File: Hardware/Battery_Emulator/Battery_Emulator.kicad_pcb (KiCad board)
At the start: 2 copper layers, 48 parts, among them J1 Vin, J2 USB4105-GF-A-060, Q1 IRFB7545PBF, SW1 Jumper, SW2 Jumper, U1 MCP4651T-103E_ST, U10 ATmega328PB-A, U2 ISO1640BDR, U3 74AHC2G125DP,125, U4 FT230XS-R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

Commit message: Update PCB
Made PCB in Kicad
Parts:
- added C22: 100n, Capacitor_SMD:C_0805_2012Metric, F.Cu at (53.3, 59.1)
- added J3: Cell1_Vout, TerminalBlock_Phoenix:TerminalBlock_Phoenix_MKDS-1,5-2-5.08_1x02_P5.08mm_Horizontal, F.Cu at (58.1, 132.7)
- J1: footprint Connector_PinSocket_2.00mm:PinSocket_1x02_P2.00mm_Vertical -> TerminalBlock_Phoenix:TerminalBlock_Phoenix_MKDS-1,5-2-5.08_1x02_P5.08mm_Horizontal
- Q1, U7: moved to B.Cu
- RV3, RV4: footprint Potentiometer_THT:Potentiometer_Bourns_PTA3043_Single_Slide -> Connector_PinHeader_2.54mm:PinHeader_1x03_P2.54mm_Vertical
- moved J2 102.7 mm to (48.5, 51.8), turned to 180 degrees
- moved R6 97.3 mm to (43.8, 58.5)
- moved C14 94.8 mm to (43.7, 60.5)
- moved RV3 91.1 mm to (69.4, 110.8)
- moved U4 89.8 mm to (48.9, 60.5), turned to 180 degrees
- moved Q1 80.1 mm to (62.3, 124.1), turned to 90 degrees
- moved C11 79.4 mm to (53.4, 62.6)
- moved C12 75.0 mm to (54.5, 70.3), turned to 0 degrees
- moved C9 74.5 mm to (51.0, 70.3), turned to 180 degrees
- moved U5 73.4 mm to (46.5, 67.8), turned to 0 degrees
- moved RV4 66.7 mm to (70.2, 94.1)
- moved C10 66.2 mm to (47.6, 70.3), turned to 0 degrees
- moved U7 66.1 mm to (62.3, 113.4), turned to 90 degrees
- moved C13 66.1 mm to (44.2, 70.3), turned to 180 degrees
- moved C21 64.8 mm to (66.8, 64.3), turned to 180 degrees
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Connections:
- J2 pad VBUS: +5V -> unconnected-(J2-PadVBUS)
- U1 pad 2: /SCL -> /Cell_1/SCL_ISO
- U1 pad 3: /SDA_cell_1-7 -> /Cell_1/SDA_ISO
- U2 pad 6: /SCL -> /Cell_1/SCL_ISO
- U2 pad 7: /SDA_cell_1-7 -> /Cell_1/SDA_ISO
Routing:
- net +5V: track 0.00 -> 84.9 mm, vias 0 -> 5
- net /Cell_1/COUT+: track 0.00 -> 55.5 mm, vias 0 -> 1
- net /Cell_1/+5V_ISO: track 0.00 -> 51.9 mm
- net /Cell_1/+9V_ISO: track 0.00 -> 38.2 mm
- net Net-(SW2-A): track 0.00 -> 32.8 mm, vias 0 -> 1
- net +12V: track 0.00 -> 27.7 mm
- net Net-(Q1-Pad1): track 0.00 -> 26.8 mm
- net /SCL: track 0.00 -> 25.3 mm, vias 0 -> 2
- net /SDA_cell_1-7: track 0.00 -> 24.9 mm
- net Net-(U8A--): track 0.00 -> 24.3 mm, vias 0 -> 1
- net Net-(SW2-C): track 0.00 -> 17.2 mm, vias 0 -> 2
- net /Cell_1/GND_ISO: track 0.00 -> 17.1 mm, vias 0 -> 7
- net /SDA: track 0.00 -> 15.9 mm, vias 0 -> 2
- net /TX: track 0.00 -> 15.2 mm, vias 0 -> 2
- net /RX: track 0.00 -> 14.1 mm, vias 0 -> 2
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- added copper zone on B.Cu, net /Cell_1/GND_ISO
- added copper zone on F.Cu, net /Cell_1/GND_ISO
- added copper zone on B.Cu, net GND
- added copper zone on F.Cu, net GND
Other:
- board outline added: 33 x 89.1 mm

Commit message: Update PCB design
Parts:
- removed U6: LM7805_TO220, Package_TO_SOT_THT:TO-220-3_Vertical
- added U9: KA78M05_TO252, Package_TO_SOT_SMD:TO-252-2, F.Cu at (59.8, 76.8)
- U5: value LM7805_TO220 -> KA78M05_TO252; footprint Package_TO_SOT_THT:TO-220-3_Vertical -> Package_TO_SOT_SMD:TO-252-2
- moved U5 38.0 mm to (57.1, 104.3), turned to 180 degrees
- moved C12 13.0 mm to (55.8, 83.3)
- moved C9 12.0 mm to (55.8, 81.3), turned to 0 degrees
- moved C1 11.3 mm to (64.6, 106.1)
- moved C10 7.80 mm to (55.1, 72.3)
- moved C13 7.52 mm to (51.7, 70.8)
- moved C21 3.85 mm to (67.2, 68.2)
- moved C22 3.85 mm to (53.8, 63.0)
- moved C4 3.85 mm to (67.3, 56.8)
- moved C5 3.85 mm to (70.0, 60.2)
- moved C8 3.85 mm to (66.5, 65.2)
- moved R3 3.85 mm to (62.1, 70.8)
- moved R4 3.85 mm to (58.2, 71.2)
- moved R5 3.85 mm to (60.2, 71.2)
- moved R6 3.85 mm to (44.2, 62.4)
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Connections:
- U5 pad 1: +12V -> /Cell_1/+9V_ISO
- U5 pad 2: GND -> /Cell_1/GND_ISO
- U5 pad 3: +5V -> /Cell_1/+5V_ISO
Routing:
- net /Cell_1/+5V_ISO: track 51.9 -> 41.8 mm, vias 0 -> 2
- net Net-(Q1-Pad1): track 26.8 -> 31.5 mm
- net GND: track 13.2 -> 17.7 mm
- net +5V: track 84.9 -> 89.0 mm, vias 5 -> 6
- net /Cell_1/+9V_ISO: track 38.2 -> 42.0 mm
- net +12V: track 27.7 -> 30.2 mm
- net /Cell_1/COUT+: track 55.5 -> 57.8 mm
- net Net-(SW2-C): track 17.2 -> 19.6 mm
- net Net-(U8A--): track 24.3 -> 26.6 mm
- net Net-(U1-P0B): track 14.1 -> 12.3 mm
- net /Cell_1/GND_ISO: track 17.1 -> 18.8 mm, vias 7 -> 9
- net /SDA_cell_1-7: track 24.9 -> 23.6 mm
- net Net-(SW1-B): track 7.61 -> 6.42 mm
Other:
- board size 33 x 89.1 mm -> 33 x 87.2 mm

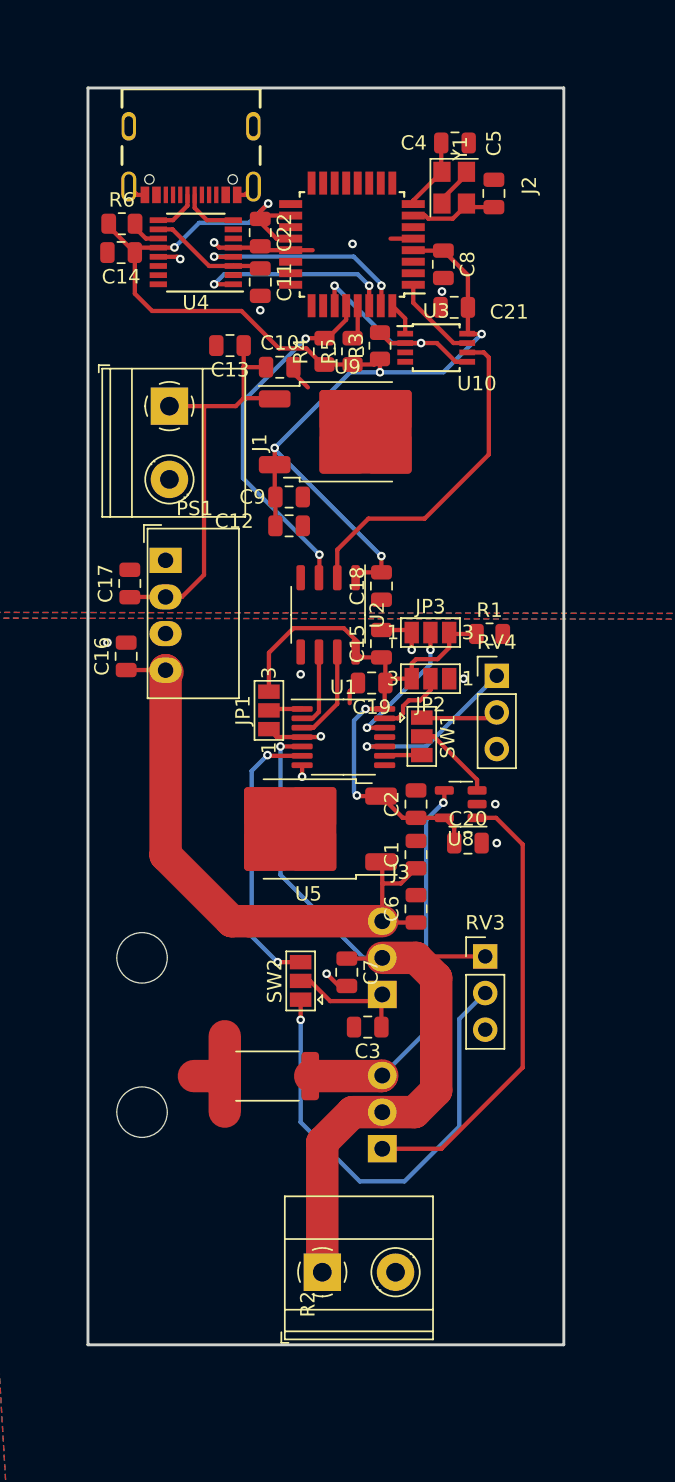
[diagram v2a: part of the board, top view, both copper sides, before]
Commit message: Update PCB
Made traces a lot larger to pass more current.
Added resistor to gate of current sink MOSFET.
Made the gerber files and ordered it at SMD lab.
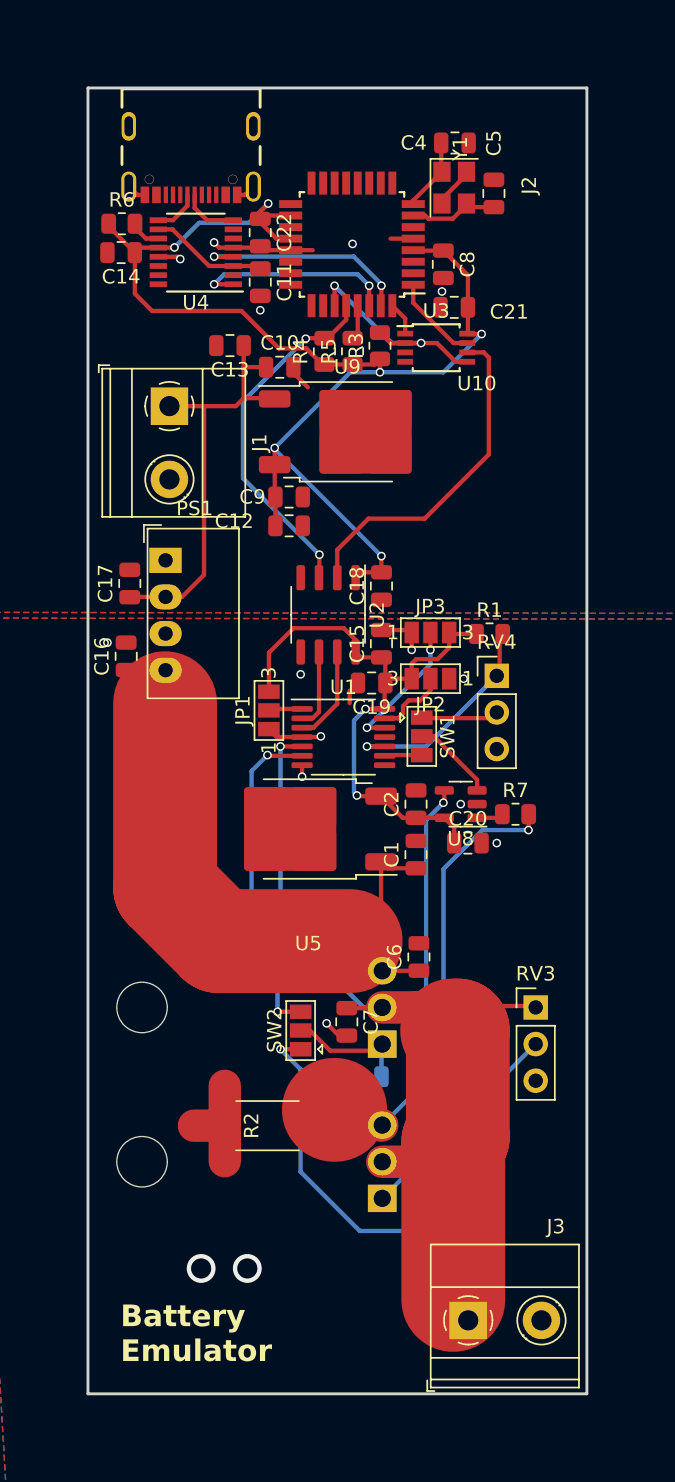
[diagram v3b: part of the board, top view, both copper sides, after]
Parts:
- added R7: 47, Resistor_SMD:R_0805_2012Metric, F.Cu at (71.5, 103.3)
- C3: moved to B.Cu
- moved J3 10.7 mm to (68.2, 138.4)
- moved RV3 4.98 mm to (72.9, 116.7)
- moved R2 3.44 mm to (54.3, 124.9)
- moved C3 3.44 mm to (61.2, 121.5)
- moved C7 3.44 mm to (59.8, 117.7)
- moved Q1 3.44 mm to (62.3, 129.9)
- moved SW2 3.44 mm to (56.6, 118.3)
- moved U7 3.44 mm to (62.3, 119.2)
- moved C6 3.35 mm to (64.8, 113.2)
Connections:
- U8 pad 1: Net-(Q1-Pad1) -> Net-(R7-Pad1)
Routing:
- net /Cell_1/COUT+: track 57.8 -> 76.5 mm
- net Net-(SW2-C): track 19.6 -> 23.0 mm
- net Net-(SW2-A): track 32.8 -> 36.1 mm
- net Net-(U1-P0B): track 12.3 -> 15.3 mm
- net /Cell_1/+9V_ISO: track 42.0 -> 44.7 mm
- net Net-(R7-Pad1): track 0.00 -> 1.85 mm
- net Net-(U8A--): track 26.6 -> 25.1 mm
- net Net-(Q1-Pad1): track 31.5 -> 32.7 mm, vias 0 -> 1
- net /Cell_1/GND_ISO: vias 9 -> 11
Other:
- board size 33 x 87.2 mm -> 34.6 x 90.6 mm
- board text added: "Battery Emulator"

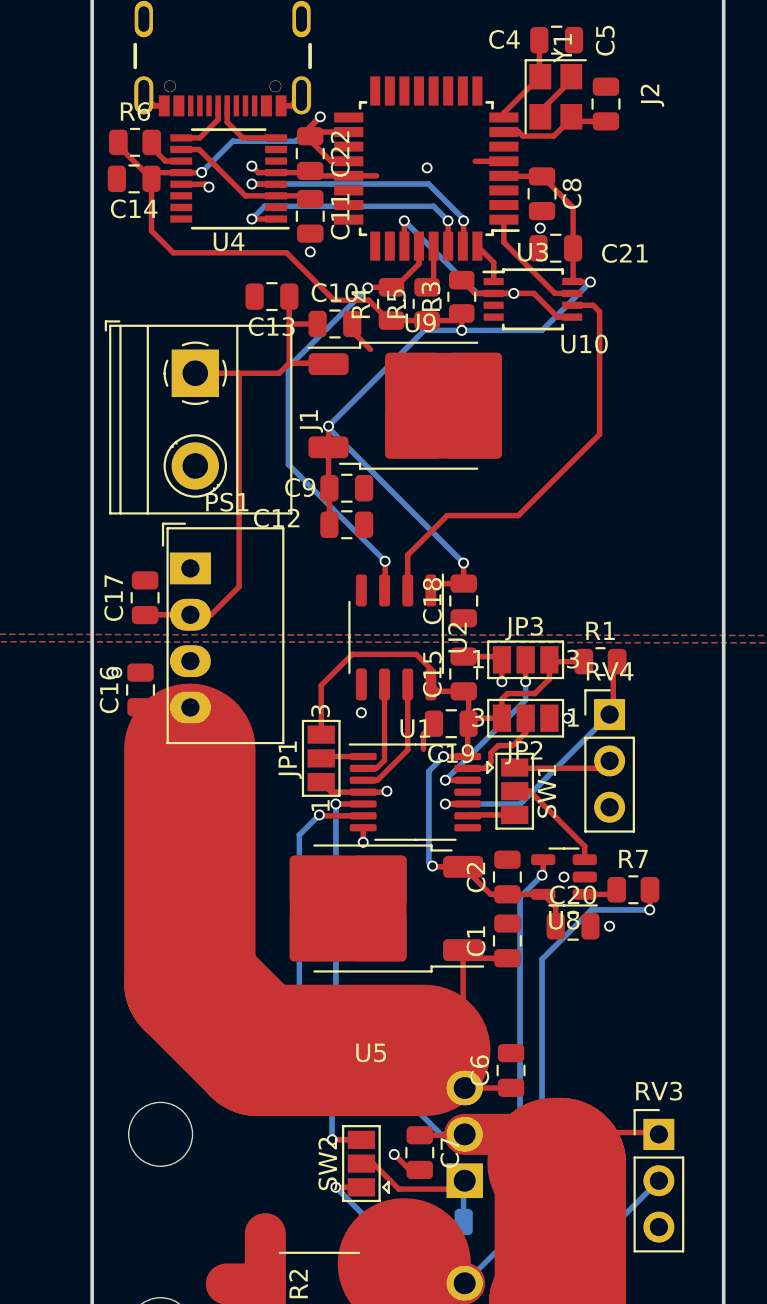
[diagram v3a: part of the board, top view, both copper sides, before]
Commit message: Update PCB
Changed via hole sizes to 0.6mm so it can be made in SMD lab
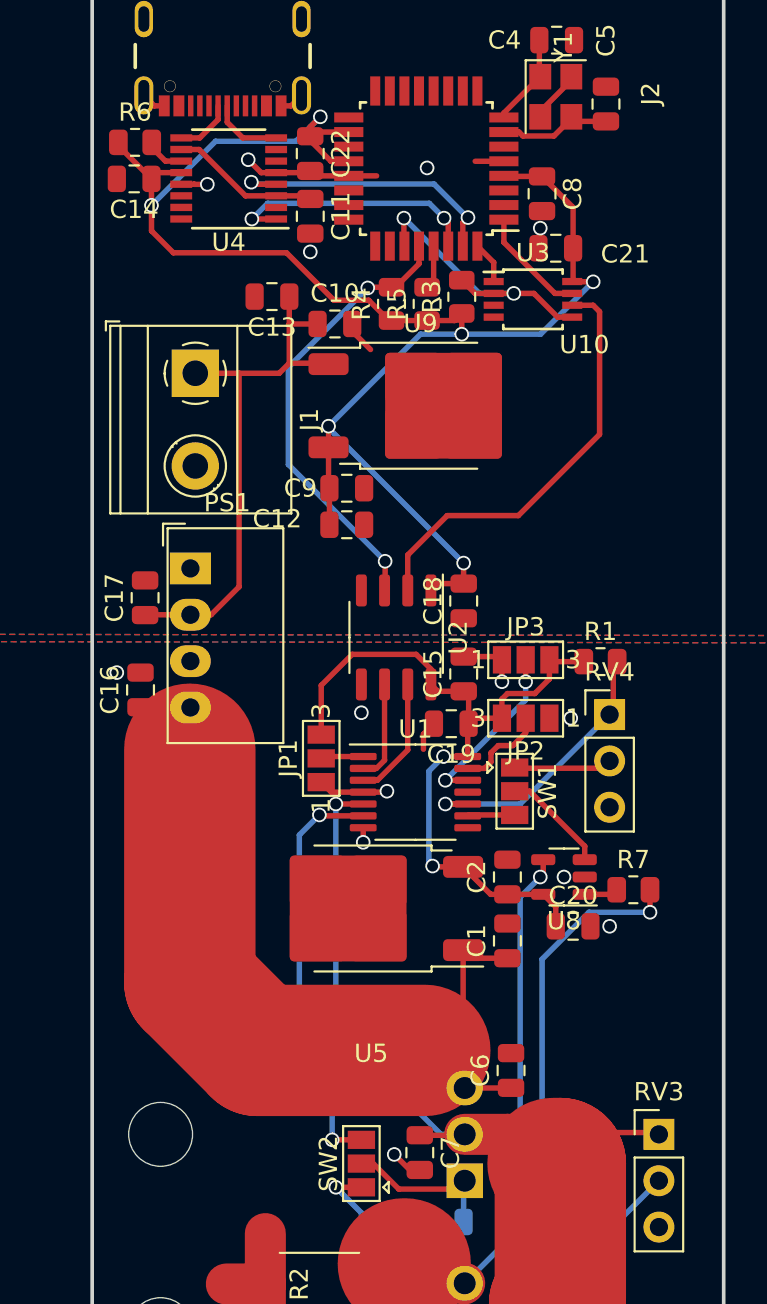
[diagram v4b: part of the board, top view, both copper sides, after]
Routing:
- net +5V: track 89.0 -> 91.9 mm
- net /TX: track 15.2 -> 15.8 mm

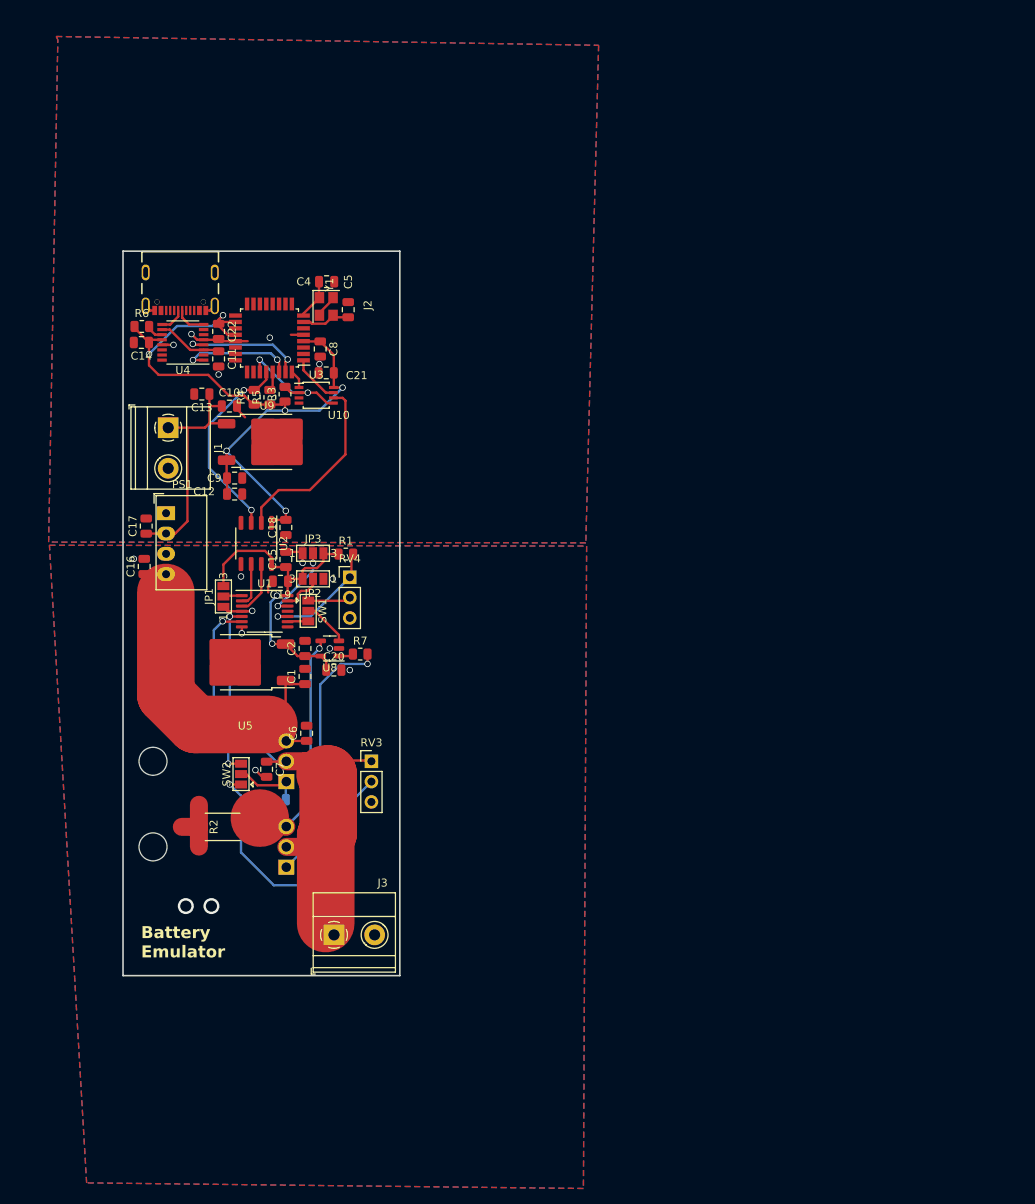
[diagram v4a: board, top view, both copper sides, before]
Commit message: Update PCB
Updated the via sizes to 0.8mm in v1
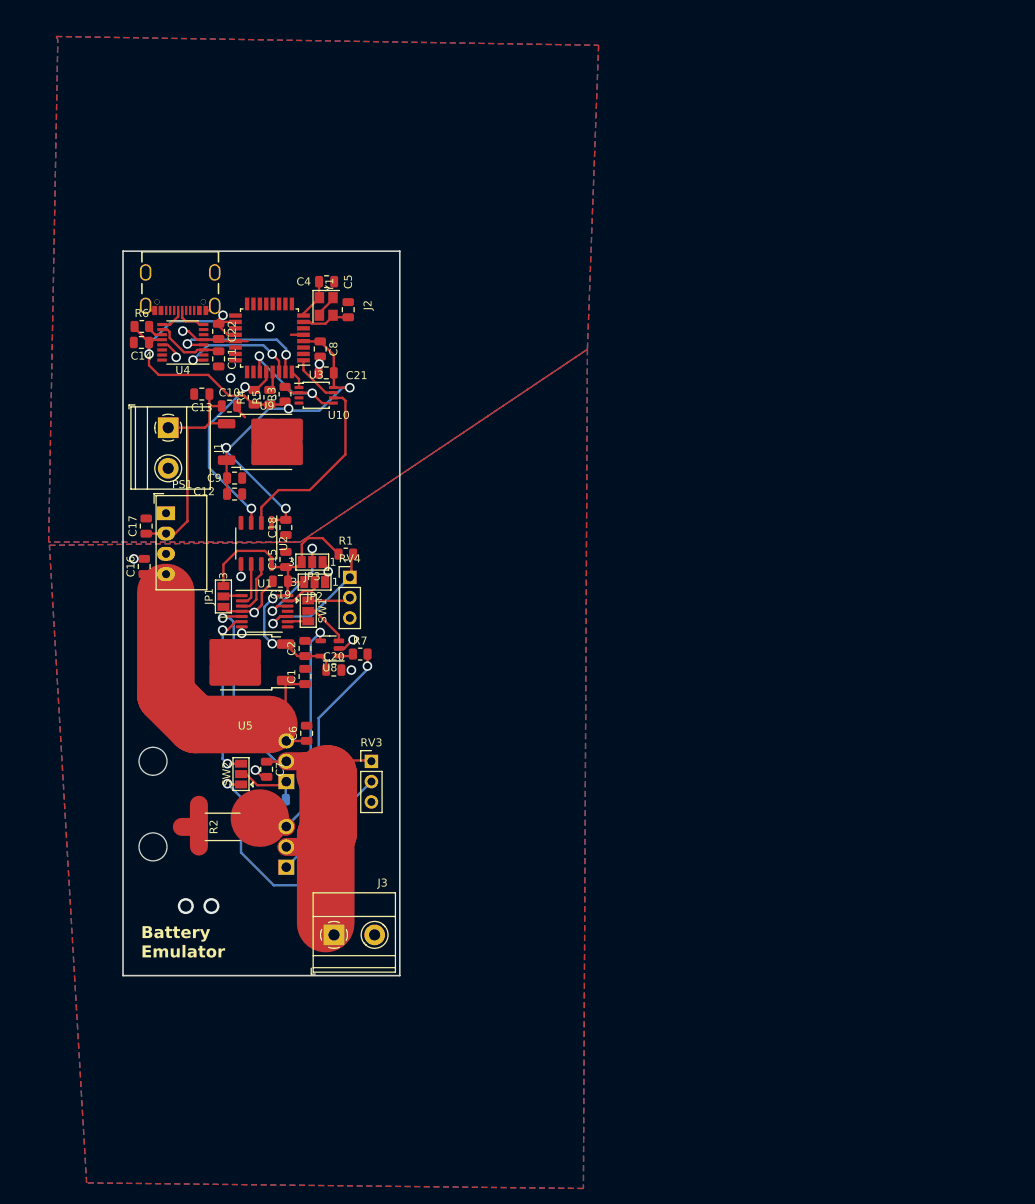
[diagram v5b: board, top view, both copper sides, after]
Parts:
- moved JP3 1.10 mm to (65.5, 91.8), turned to 180 degrees
- moved JP2 0.45 mm to (65.8, 94.3)
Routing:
- net /Cell_1/GND_ISO: track 18.8 -> 24.5 mm, vias 11 -> 10
- net /Cell_1/A2: track 9.65 -> 13.8 mm
- net /Cell_1/+5V_ISO: track 41.8 -> 45.8 mm
- net +5V: track 91.9 -> 95.4 mm
- net GND: track 17.9 -> 20.4 mm
- net /TX: track 15.8 -> 18.0 mm
- net Net-(U8A--): track 25.1 -> 27.2 mm
- net Net-(Q1-Pad1): track 32.8 -> 30.8 mm
- net Net-(U1-P0B): track 15.3 -> 17.3 mm
- net /Cell_1/COUT+: track 76.5 -> 78.1 mm
- net Net-(SW2-C): track 23.0 -> 21.5 mm
- net /SDA: track 16.2 -> 17.7 mm
- net /RX: track 14.2 -> 15.0 mm
- net Net-(U4-3V3OUT): track 8.21 -> 8.89 mm
- net /SCL: track 24.9 -> 25.5 mm
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
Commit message: PCB-update for production
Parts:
- C7: moved to B.Cu
- moved C7 5.59 mm to (65.3, 116.7), turned to 0 degrees
- moved C3 4.63 mm to (65.3, 119.2), turned to 0 degrees
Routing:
- net /Cell_1/GND_ISO: track 24.5 -> 30.5 mm, vias 10 -> 9
- net +5V: track 95.4 -> 100.6 mm
- net /Cell_1/+5V_ISO: track 45.8 -> 48.7 mm
- net /Cell_1/COUT+: track 78.1 -> 80.7 mm, vias 1 -> 2
- net Net-(U8A--): track 27.2 -> 28.9 mm
- net /RX: track 15.0 -> 16.3 mm
- net Net-(U1-P0B): track 17.3 -> 18.4 mm
- net GND: track 20.4 -> 21.4 mm, vias 5 -> 6
- net /TX: track 18.0 -> 18.9 mm
- net Net-(SW2-A): track 36.7 -> 37.5 mm
- net Net-(SW2-B): track 8.80 -> 8.23 mm
- net /Cell_1/+9V_ISO: track 44.7 -> 44.8 mm, vias 0 -> 1
- net +12V: vias 0 -> 1
